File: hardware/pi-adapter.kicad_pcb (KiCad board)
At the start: 2 copper layers, 64 x 56 mm, 37 parts, among them P1 CONN_01X04, P10 CONN_01X04, P11 CONN_01X04, P12 CONN_01X04, P13 CONN_01X04, P14 CONN_01X04, P15 CONN_01X04, P16 CONN_01X04, P2 CONN_01X04, P20 CONN_02X20, P21 CONN_01X03, P22 CONN_01X06, P23 CONN_01X03, P3 CONN_01X04, P30 +5V, P31 GND, P4 CONN_01X04, P40 CONN_01X01, P41 CONN_01X01, P43 CONN_01X01, P5 CONN_01X04, P6 CONN_01X04, P7 CONN_01X04, P8 CONN_01X04, P9 CONN_01X04, U1 74HCT245, U2 74HCT245, U3 74HCT245, U4 74HCT245

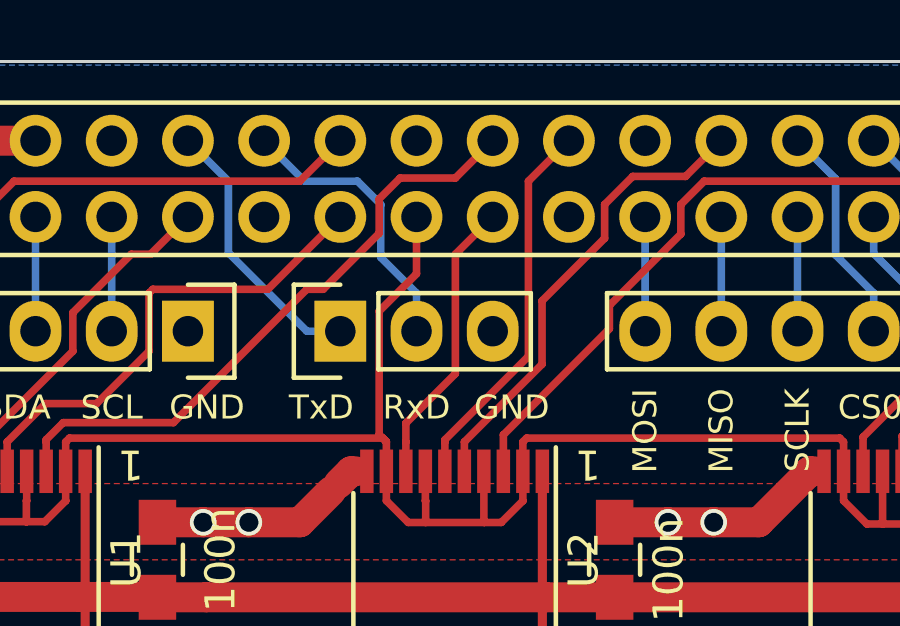
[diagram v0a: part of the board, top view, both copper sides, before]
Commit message: o Turn around serial connector to have the gound pin on the (square)   pin 1 on the header.
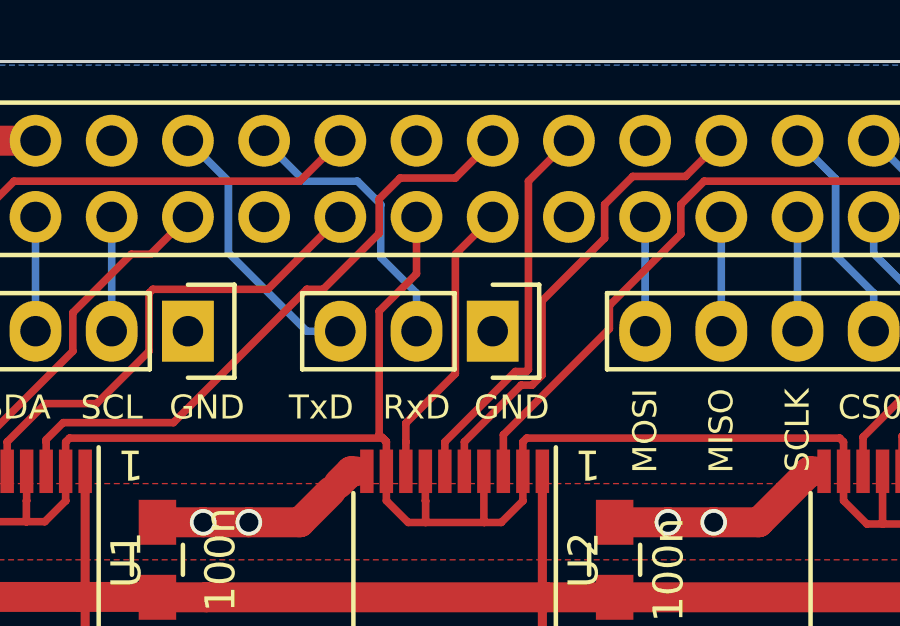
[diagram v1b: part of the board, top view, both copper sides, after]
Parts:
- moved P23 5.08 mm to (125.7, 47.0), turned to 270 degrees
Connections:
- P23 pad 1: Net-(P20-Pad8) -> GND
- P23 pad 3: GND -> Net-(P20-Pad8)
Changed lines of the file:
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@@
-(kicad_pcb (version 4) (host pcbnew "(2016-02-20 BZR 6576, Git d7e2ffe)-product")
+(kicad_pcb (version 4) (host pcbnew "(2015-08-05 BZR 6054, Git 5c8efeb)-product")
   (general
     (links 150)
@@
     (thickness 1.6)
     (drawings 84)
-    (tracks 574)
+    (tracks 577)
     (zones 0)
     (modules 37)
@@
       (hpglpenspeed 20)
       (hpglpendiameter 15)
+      (hpglpenoverlay 2)
       (psnegative false)
       (psa4output false)
@@
   )
   (module Pin_Headers:Pin_Header_Straight_1x03 (layer F.Cu)
-    (at 120.65 46.99 90)
+    (at 125.73 46.99 270)
     (descr "Through hole pin header")
     (tags "pin header")
-    (fp_text reference P23 (at -0.254 -2.286 90) (layer F.SilkS) hide
-      (effects (font (size 1 1) (thickness 0.15)))
-    )
-    (fp_text value CONN_01X03 (at 0 -3.1 90) (layer F.Fab)
+    (fp_text reference P23 (at -0.254 -2.286 270) (layer F.SilkS) hide
+      (effects (font (size 1 1) (thickness 0.15)))
+    )
+    (fp_text value CONN_01X03 (at 0 -3.1 270) (layer F.Fab)
       (effects (font (size 1 1) (thickness 0.15)))
     )
@@
     (fp_line (start -1.55 0) (end -1.55 -1.55) (layer F.SilkS) (width 0.15))
     (fp_line (start -1.55 -1.55) (end 1.55 -1.55) (layer F.SilkS) (width 0.15))
-    (pad 1 thru_hole rect (at 0 0 90) (size 2.032 1.7272) (drill 1.016) (layers *.Cu *.Mask F.SilkS)
+    (pad 1 thru_hole rect (at 0 0 270) (size 2.032 1.7272) (drill 1.016) (layers *.Cu *.Mask F.SilkS)
+      (net 2 GND))
+    (pad 2 thru_hole oval (at 0 2.54 270) (size 2.032 1.7272) (drill 1.016) (layers *.Cu *.Mask F.SilkS)
+      (net 4 "Net-(P20-Pad10)"))
+    (pad 3 thru_hole oval (at 0 5.08 270) (size 2.032 1.7272) (drill 1.016) (layers *.Cu *.Mask F.SilkS)
       (net 61 "Net-(P20-Pad8)"))
-    (pad 2 thru_hole oval (at 0 2.54 90) (size 2.032 1.7272) (drill 1.016) (layers *.Cu *.Mask F.SilkS)
-      (net 4 "Net-(P20-Pad10)"))
-    (pad 3 thru_hole oval (at 0 5.08 90) (size 2.032 1.7272) (drill 1.016) (layers *.Cu *.Mask F.SilkS)
-      (net 2 GND))
     (model Pin_Headers.3dshapes/Pin_Header_Straight_1x03.wrl
       (at (xyz 0 -0.1 0))
@@
   (segment (start 120.079011 45.592999) (end 119.532403 45.592999) (width 0.254) (layer F.Cu) (net 11))
   (segment (start 119.532403 45.592999) (end 115.087402 50.038) (width 0.254) (layer F.Cu) (net 11))
+  (segment (start 126.920601 48.267601) (end 126.855201 48.333001) (width 0.254) (layer F.Cu) (net 12))
+  (segment (start 128.27 40.64) (end 126.920601 41.989399) (width 0.254) (layer F.Cu) (net 12))
+  (segment (start 126.920601 41.989399) (end 126.920601 48.267601) (width 0.254) (layer F.Cu) (net 12))
   (segment (start 124.135 50.681) (end 124.135 51.66) (width 0.254) (layer F.Cu) (net 12))
-  (segment (start 126.92061 47.826954) (end 124.135 50.612564) (width 0.254) (layer F.Cu) (net 12))
-  (segment (start 126.92061 41.98939) (end 126.92061 47.826954) (width 0.254) (layer F.Cu) (net 12))
-  (segment (start 124.135 50.612564) (end 124.135 50.681) (width 0.254) (layer F.Cu) (net 12))
-  (segment (start 128.27 40.64) (end 126.92061 41.98939) (width 0.254) (layer F.Cu) (net 12))
-  (segment (start 129.460601 43.894399) (end 127.374621 45.980379) (width 0.254) (layer F.Cu) (net 13))
-  (segment (start 127.374621 45.980379) (end 127.374621 48.091379) (width 0.254) (layer F.Cu) (net 13))
-  (segment (start 127.374621 48.091379) (end 124.785 50.681) (width 0.254) (layer F.Cu) (net 13))
+  (segment (start 126.855201 48.333001) (end 126.482999 48.333001) (width 0.254) (layer F.Cu) (net 12))
+  (segment (start 126.482999 48.333001) (end 124.135 50.681) (width 0.254) (layer F.Cu) (net 12))
   (segment (start 124.785 50.681) (end 124.785 51.66) (width 0.254) (layer F.Cu) (net 13))
+  (segment (start 127.374611 48.455658) (end 127.043258 48.787011) (width 0.254) (layer F.Cu) (net 13))
+  (segment (start 127.374611 45.980389) (end 127.374611 48.455658) (width 0.254) (layer F.Cu) (net 13))
+  (segment (start 129.460601 43.894399) (end 127.374611 45.980389) (width 0.254) (layer F.Cu) (net 13))
+  (segment (start 129.460601 42.767309) (end 129.460601 43.894399) (width 0.254) (layer F.Cu) (net 13))
+  (segment (start 130.397309 41.830601) (end 129.460601 42.767309) (width 0.254) (layer F.Cu) (net 13))
+  (segment (start 126.678989 48.787011) (end 124.785 50.681) (width 0.254) (layer F.Cu) (net 13))
+  (segment (start 127.043258 48.787011) (end 126.678989 48.787011) (width 0.254) (layer F.Cu) (net 13))
+  (segment (start 132.159399 41.830601) (end 130.397309 41.830601) (width 0.254) (layer F.Cu) (net 13))
   (segment (start 133.35 40.64) (end 132.159399 41.830601) (width 0.254) (layer F.Cu) (net 13))
-  (segment (start 132.159399 41.830601) (end 130.397309 41.830601) (width 0.254) (layer F.Cu) (net 13))
-  (segment (start 130.397309 41.830601) (end 129.460601 42.767309) (width 0.254) (layer F.Cu) (net 13))
-  (segment (start 129.460601 42.767309) (end 129.460601 43.894399) (width 0.254) (layer F.Cu) (net 13))
   (segment (start 139.62061 48.97439) (end 138.075 50.52) (width 0.254) (layer F.Cu) (net 14))
   (segment (start 138.075 50.52) (end 138.075 51.66) (width 0.254) (layer F.Cu) (net 14))
@@
   (segment (start 133.35 43.18) (end 133.35 46.99) (width 0.254) (layer B.Cu) (net 59))
   (segment (start 135.89 43.18) (end 135.89 46.99) (width 0.254) (layer B.Cu) (net 60))
+  (segment (start 119.5324 46.99) (end 120.65 46.99) (width 0.254) (layer B.Cu) (net 61))
   (segment (start 115.57 40.64) (end 116.919399 41.989399) (width 0.254) (layer B.Cu) (net 61))
   (segment (start 116.919399 41.989399) (end 116.919399 44.376999) (width 0.254) (layer B.Cu) (net 61))
   (segment (start 116.919399 44.376999) (end 119.5324 46.99) (width 0.254) (layer B.Cu) (net 61))
-  (segment (start 119.5324 46.99) (end 120.65 46.99) (width 0.254) (layer B.Cu) (net 61))
   (zone (net 55) (net_name Fused5V) (layer F.Cu) (hatch edge 0.508)
     (connect_pads yes (clearance 0.508))
